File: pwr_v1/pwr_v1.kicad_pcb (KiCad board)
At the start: 2 copper layers, 166 x 166 mm, 34 parts, among them J1 Conn_01x02, J2 Conn_02x03_Counter_Clockwise, J3 Conn_01x02, J4 Conn_01x02, J5 Conn_01x02, M1 Conn_01x08_Socket, U1 LM2576S-5, U2 LM2576S-12

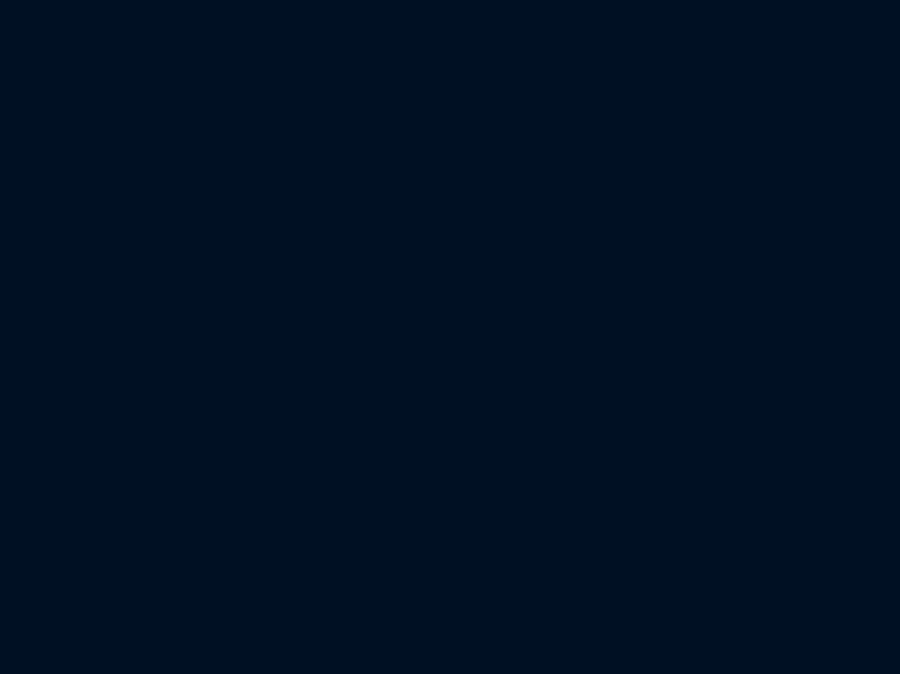
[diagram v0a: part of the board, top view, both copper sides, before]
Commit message: IMU layout updated
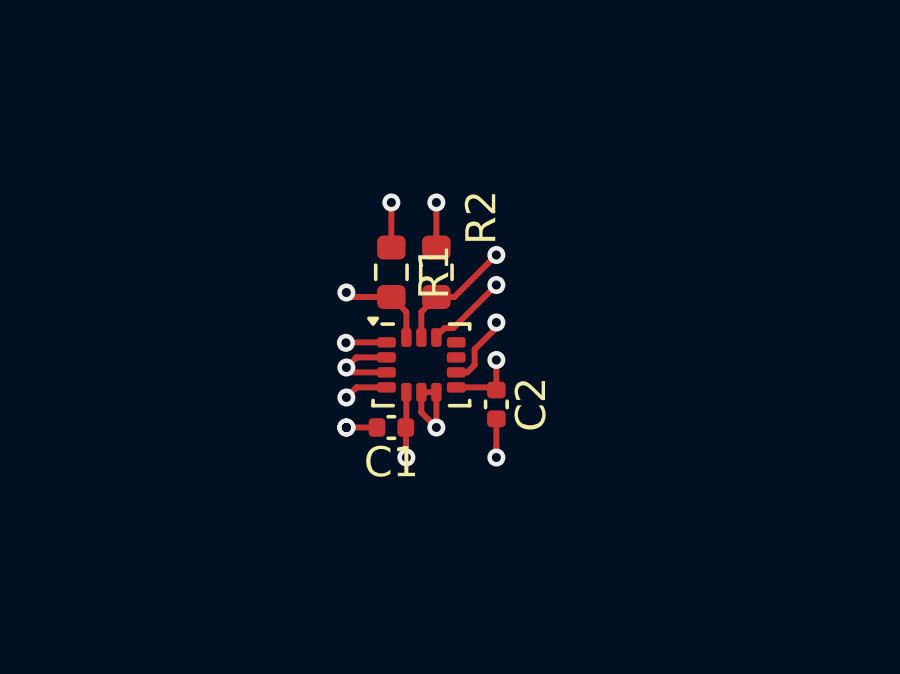
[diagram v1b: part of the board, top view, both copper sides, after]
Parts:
- added C1: 100nF, Capacitor_SMD:C_0402_1005Metric, F.Cu at (149.5, 102.5)
- added C2: 100nF, Capacitor_SMD:C_0402_1005Metric, F.Cu at (153.0, 101.7)
- added R1: 1k, Resistor_SMD:R_0603_1608Metric, F.Cu at (149.5, 97.3)
- added R2: 1k, Resistor_SMD:R_0603_1608Metric, F.Cu at (151.0, 97.3)
- added U1: LSM6DSLTR, Package_LGA:LGA-14_3x2.5mm_P0.5mm_LayoutBorder3x4y, F.Cu at (150.5, 100.4)
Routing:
- net (no net): track 0.00 -> 23.3 mm, vias 0 -> 10
- net GND: track 0.00 -> 8.58 mm, vias 124 -> 129

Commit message: Schematic and layout updated
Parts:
- removed the C1 at (149.5, 102.5)
- removed the C2 at (153.0, 101.7)
- removed D3: 1N5821, Diode_THT:D_DO-201AD_P15.24mm_Horizontal
- removed L3: 47uH, Inductor_SMD:L_0805_2012Metric
- removed REF** (x2): PinHeader_2x36_P2.54mm_Vertical_SMD, Connector_PinHeader_2.54mm:PinHeader_2x36_P2.54mm_Vertical_SMD
- removed the U1 at (150.5, 100.4)
- removed U_M1: MCT8316Z0TQRGFRQ1, MTR:RGF0040E-IPC_B
- added 1L1: 47uH, Inductor_SMD:L_0805_2012Metric, B.Cu at (147.1, 48.9)
- added 1U1: MCT8316Z0TQRGFRQ1, MTR:RGF0040E-IPC_B, B.Cu at (140.5, 52.7)
- added 2C1: 100nF, Capacitor_SMD:C_0805_2012Metric, F.Cu at (26.6, 54.5)
- added 2C2: 47nF, Capacitor_SMD:C_0603_1608Metric, F.Cu at (22.4, 47.3)
- added 2C3: 1uF, Capacitor_SMD:C_0402_1005Metric, F.Cu at (30.3, 57.0)
- added 2C4: 0u1F, Capacitor_SMD:C_0603_1608Metric, F.Cu at (22.4, 49.8)
- added 2C5: 22uF, Capacitor_SMD:C_2220_5750Metric, F.Cu at (28.6, 49.5)
- added 2C6: 22uF, Capacitor_SMD:C_0603_1608Metric, F.Cu at (22.4, 52.3)
- added 2C7: 1uF, Capacitor_SMD:C_0402_1005Metric, F.Cu at (30.3, 59.0)
- added 2L1: 47uH, Inductor_SMD:L_0805_2012Metric, F.Cu at (30.2, 38.7)
- added 2R1: 5k1, Resistor_SMD:R_0603_1608Metric_Pad0.98x0.95mm_HandSolder, F.Cu at (31.1, 54.2)
- added 2R2: 5k1, Resistor_SMD:R_0603_1608Metric, F.Cu at (22.4, 54.8)
- added 2R3: 27k, Resistor_SMD:R_0603_1608Metric, F.Cu at (22.4, 57.3)
- added 2R4: 20k, Resistor_SMD:R_0603_1608Metric, F.Cu at (22.4, 59.8)
- added 2R5: 1M, Resistor_SMD:R_0805_2012Metric, F.Cu at (26.6, 57.5)
- added 2R6: 47k, Resistor_SMD:R_0402_1005Metric, F.Cu at (29.4, 41.1)
- added 2R7: 22k, Resistor_SMD:R_0402_1005Metric, F.Cu at (29.4, 43.1)
- added 2U1: MCT8316Z0TQRGFRQ1, MTR:RGF0040E-IPC_B, F.Cu at (24.6, 41.7)
- added 3C1: 100nF, Capacitor_SMD:C_0805_2012Metric, F.Cu at (49.4, 54.5)
- added 3C2: 47nF, Capacitor_SMD:C_0603_1608Metric, F.Cu at (45.2, 47.3)
- added 3C3: 1uF, Capacitor_SMD:C_0402_1005Metric, F.Cu at (53.0, 57.0)
- added 3C4: 0u1F, Capacitor_SMD:C_0603_1608Metric, F.Cu at (45.2, 49.8)
- added 3C5: 22uF, Capacitor_SMD:C_2220_5750Metric, F.Cu at (51.4, 49.5)
- added 3C6: 22uF, Capacitor_SMD:C_0603_1608Metric, F.Cu at (45.2, 52.3)
- added 3C7: 1uF, Capacitor_SMD:C_0402_1005Metric, F.Cu at (53.0, 59.0)
- added 3L1: 47uH, Inductor_SMD:L_0805_2012Metric, F.Cu at (53.0, 38.7)
- added 3R1: 5k1, Resistor_SMD:R_0603_1608Metric_Pad0.98x0.95mm_HandSolder, F.Cu at (53.8, 54.2)
- added 3R2: 5k1, Resistor_SMD:R_0603_1608Metric, F.Cu at (45.2, 54.8)
- added 3R3: 27k, Resistor_SMD:R_0603_1608Metric, F.Cu at (45.2, 57.3)
- added 3R4: 20k, Resistor_SMD:R_0603_1608Metric, F.Cu at (45.2, 59.8)
- added 3R5: 1M, Resistor_SMD:R_0805_2012Metric, F.Cu at (49.4, 57.5)
- added 3R6: 47k, Resistor_SMD:R_0402_1005Metric, F.Cu at (52.1, 41.1)
- added 3R7: 22k, Resistor_SMD:R_0402_1005Metric, F.Cu at (52.1, 43.1)
- added 3U1: MCT8316Z0TQRGFRQ1, MTR:RGF0040E-IPC_B, F.Cu at (47.3, 41.7)
- added 4C1: 100nF, Capacitor_SMD:C_0805_2012Metric, F.Cu at (49.4, 28.7)
- added 4C2: 47nF, Capacitor_SMD:C_0603_1608Metric, F.Cu at (45.2, 21.5)
- added 4C3: 1uF, Capacitor_SMD:C_0402_1005Metric, F.Cu at (53.0, 31.2)
- added 4C4: 0u1F, Capacitor_SMD:C_0603_1608Metric, F.Cu at (45.2, 24.0)
- added 4C5: 22uF, Capacitor_SMD:C_2220_5750Metric, F.Cu at (51.4, 23.7)
- added 4C6: 22uF, Capacitor_SMD:C_0603_1608Metric, F.Cu at (45.2, 26.5)
- added 4C7: 1uF, Capacitor_SMD:C_0402_1005Metric, F.Cu at (53.0, 33.2)
- added 4L1: 47uH, Inductor_SMD:L_0805_2012Metric, F.Cu at (53.0, 12.9)
- added 4R1: 5k1, Resistor_SMD:R_0603_1608Metric_Pad0.98x0.95mm_HandSolder, F.Cu at (53.8, 28.5)
- added 4R2: 5k1, Resistor_SMD:R_0603_1608Metric, F.Cu at (45.2, 29.1)
- added 4R3: 27k, Resistor_SMD:R_0603_1608Metric, F.Cu at (45.2, 31.6)
- added 4R4: 20k, Resistor_SMD:R_0603_1608Metric, F.Cu at (45.2, 34.1)
- added 4R5: 1M, Resistor_SMD:R_0805_2012Metric, F.Cu at (49.4, 31.7)
- added 4R6: 47k, Resistor_SMD:R_0402_1005Metric, F.Cu at (52.1, 15.3)
- added 4R7: 22k, Resistor_SMD:R_0402_1005Metric, F.Cu at (52.1, 17.3)
- added 4U1: MCT8316Z0TQRGFRQ1, MTR:RGF0040E-IPC_B, F.Cu at (47.3, 15.9)
- added 5C1: 100nF, Capacitor_SMD:C_0805_2012Metric, F.Cu at (26.6, 28.7)
- added 5C2: 47nF, Capacitor_SMD:C_0603_1608Metric, F.Cu at (22.4, 21.5)
- added 5C3: 1uF, Capacitor_SMD:C_0402_1005Metric, F.Cu at (30.3, 31.2)
- added 5C4: 0u1F, Capacitor_SMD:C_0603_1608Metric, F.Cu at (22.4, 24.0)
- added 5C5: 22uF, Capacitor_SMD:C_2220_5750Metric, F.Cu at (28.6, 23.7)
- added 5C6: 22uF, Capacitor_SMD:C_0603_1608Metric, F.Cu at (22.4, 26.5)
- added 5C7: 1uF, Capacitor_SMD:C_0402_1005Metric, F.Cu at (30.3, 33.2)
- added 5L1: 47uH, Inductor_SMD:L_0805_2012Metric, F.Cu at (30.2, 12.9)
- added 5R1: 5k1, Resistor_SMD:R_0603_1608Metric_Pad0.98x0.95mm_HandSolder, F.Cu at (31.1, 28.5)
- added 5R2: 5k1, Resistor_SMD:R_0603_1608Metric, F.Cu at (22.4, 29.1)
- added 5R3: 27k, Resistor_SMD:R_0603_1608Metric, F.Cu at (22.4, 31.6)
- added 5R4: 20k, Resistor_SMD:R_0603_1608Metric, F.Cu at (22.4, 34.1)
- added 5R5: 1M, Resistor_SMD:R_0805_2012Metric, F.Cu at (26.6, 31.7)
- added 5R6: 47k, Resistor_SMD:R_0402_1005Metric, F.Cu at (29.4, 15.3)
- added 5R7: 22k, Resistor_SMD:R_0402_1005Metric, F.Cu at (29.4, 17.3)
- added 5U1: MCT8316Z0TQRGFRQ1, MTR:RGF0040E-IPC_B, F.Cu at (24.6, 15.9)
- added BAT1: Conn_01x02, TerminalBlock_4Ucon:TerminalBlock_4Ucon_1x02_P3.50mm_Horizontal, F.Cu at (61.1, 48.5)
- added C12: 100nF, Capacitor_SMD:C_0402_1005Metric, F.Cu at (149.4, 102.5)
- added C13: 100nF, Capacitor_SMD:C_0402_1005Metric, F.Cu at (153.0, 101.8)
- added CN11: Conn_02x36_Odd_Even, Connector_PinHeader_2.54mm:PinHeader_2x36_P2.54mm_Vertical_SMD, F.Cu at (131.8, 121.0)
- added CN12: Conn_02x36_Odd_Even, Connector_PinHeader_2.54mm:PinHeader_2x36_P2.54mm_Vertical_SMD, F.Cu at (177.2, 116.0)
- added D1: 1N5821, Diode_THT:D_DO-201AD_P15.24mm_Horizontal, F.Cu at (60.4, 40.7)
- added M2: Conn_01x08_Socket, Connector_PinHeader_2.54mm:PinHeader_1x08_P2.54mm_Vertical_SMD_Pin1Left, F.Cu at (16.4, 48.5)
- added M3: Conn_01x08_Socket, Connector_PinHeader_2.54mm:PinHeader_1x08_P2.54mm_Vertical_SMD_Pin1Left, F.Cu at (39.2, 48.5)
- added M4: Conn_01x08_Socket, Connector_PinHeader_2.54mm:PinHeader_1x08_P2.54mm_Vertical_SMD_Pin1Left, F.Cu at (39.2, 22.8)
- added M5: Conn_01x08_Socket, Connector_PinHeader_2.54mm:PinHeader_1x08_P2.54mm_Vertical_SMD_Pin1Left, F.Cu at (16.4, 22.8)
- added R3: 1k, Resistor_SMD:R_0603_1608Metric, F.Cu at (1.50, 0.76)
- added U4: LSM6DSLTR, Package_LGA:LGA-14_3x2.5mm_P0.5mm_LayoutBorder3x4y, F.Cu at (150.5, 100.5)
- 1C1: footprint Capacitor_SMD:C_0805_2012Metric -> Capacitor_SMD:C_0402_1005Metric
- 1C2, 1C4, 1C6: footprint Capacitor_SMD:C_0603_1608Metric -> Capacitor_SMD:C_0402_1005Metric
- 1C7: footprint Capacitor_SMD:C_1206_3216Metric -> Capacitor_SMD:C_0402_1005Metric
- C3: footprint Capacitor_SMD:CP_Elec_10x10.5 -> Capacitor_SMD:CP_Elec_8x10.5
- C4: footprint Capacitor_SMD:CP_Elec_8x10.5 -> Capacitor_SMD:CP_Elec_10x10.5
- L1: footprint Inductor_SMD:L_TaiTech_TMPC1265_13.5x12.5mm -> Inductor_SMD:L_Sunlord_MWSA1206S-101
- L2: footprint Inductor_SMD:L_Sunlord_MWSA1206S-101 -> Inductor_SMD:L_TaiTech_TMPC1265_13.5x12.5mm
- R1: value 1k -> R_Small_US
- moved 1C7 194.2 mm to (135.4, 55.2)
- moved 1C3 193.5 mm to (146.3, 54.2)
- moved 1C4 192.0 mm to (145.1, 55.2)
- moved 1C2 192.0 mm to (146.4, 51.9), turned to 180 degrees
- moved 1C6 191.5 mm to (146.6, 46.4), turned to 180 degrees
- moved 1R3 190.8 mm to (139.9, 42.9), turned to 0 degrees
- moved 1R2 189.6 mm to (145.2, 44.0), turned to -90 degrees
- moved 1C1 189.3 mm to (140.3, 46.0), turned to 180 degrees
- moved 1R7 189.1 mm to (136.9, 45.5)
- moved 1R5 188.9 mm to (132.8, 53.0), turned to 180 degrees
- moved 1R6 188.9 mm to (135.7, 45.5)
- moved 1R1 188.1 mm to (131.8, 56.0), turned to -90 degrees
- moved 1R4 186.9 mm to (139.9, 44.6), turned to 180 degrees
- moved 1C5 186.4 mm to (150.5, 58.1), turned to -90 degrees
- moved M1 177.6 mm to (163.7, 50.4)
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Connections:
- net /MotorDrivers/AVDD renamed /MotorDriver1/AVDD
- net /MotorDrivers/SW_BK renamed /MotorDriver1/SW_BK
- net /MotorDrivers/VM renamed +24V
- net 12V renamed +12V
- 1C1 pad 2: GNDREF -> GND
- 1C4 pad 2: GNDREF -> GND
- 1C5 pad 2: GNDREF -> GND
- 1C6 pad 2: GNDREF -> /MotorDriver1/GND_BK
- 1C7 pad 2: GNDREF -> GND
- 1R1 pad 2: /MotorDrivers/nFault -> +5V
- 1R2 pad 2: /MotorDrivers/FGOUT -> /MotorDriver1/FGOUT
- 1R4 pad 2: GNDREF -> GND
- C3 pad 1: 5V -> +5V
- L1 pad 2: 5V -> +5V
- M1 pad 1: /MotorDrivers/U -> /MotorDriver1/U
- M1 pad 2: /MotorDrivers/V -> /MotorDriver1/V
- M1 pad 3: /MotorDrivers/W -> /MotorDriver1/W
- M1 pad 4: GNDREF -> /MotorDriver1/GND_BK
- M1 pad 5: /MotorDrivers/H2 -> /MotorDriver1/H2
- M1 pad 6: /MotorDrivers/H1 -> /MotorDriver1/H1
- M1 pad 7: /MotorDrivers/H3 -> /MotorDriver1/H3
- R1 pad 1: (no net) -> /Battery Supervisor/B1
- R1 pad 2: (no net) -> Net-(D3-A)
- R2 pad 1: (no net) -> /IMU/3V3
- R2 pad 2: (no net) -> /IMU/SCL
- U1 pad 4: 5V -> +5V
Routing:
- net /MotorDriver1/AVDD: track 0.00 -> 25.4 mm, vias 0 -> 5
- net (no net): track 23.3 -> 0.00 mm, vias 10 -> 0
- net +24V: track 0.00 -> 13.9 mm
- net GND: track 8.58 -> 21.8 mm, vias 129 -> 136
- net +5V: track 0.00 -> 9.76 mm, vias 0 -> 1
- net /MotorDriver1/GND_BK: track 0.00 -> 7.00 mm
- net Net-(1U1-ILIM): track 0.00 -> 6.38 mm
- net /IMU/3V3: track 0.00 -> 6.31 mm, vias 0 -> 3
- net Net-(1U1-SLEW): track 0.00 -> 5.75 mm
- net /MotorDriver1/W: track 0.00 -> 5.70 mm
- net /MotorDriver1/V: track 0.00 -> 5.70 mm
- net /MotorDriver1/U: track 0.00 -> 5.70 mm
- net /MotorDriver1/FGOUT: track 0.00 -> 5.64 mm
- net Net-(1U1-ADVANCE): track 0.00 -> 5.22 mm
- net /MotorDriver1/SW_BK: track 0.00 -> 5.19 mm, vias 0 -> 1
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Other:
- copper layers 2 -> 6

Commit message: Sch and Layout updated; Added batt sup ckt, placed and routed all motor drivers.
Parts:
- removed J1: Conn_01x02, TerminalBlock_4Ucon:TerminalBlock_4Ucon_1x02_P3.50mm_Horizontal
- removed J2: Conn_02x03_Counter_Clockwise, Connector_PinHeader_2.54mm:PinHeader_1x02_P2.54mm_Vertical
- removed J3, J4, J5: Conn_01x02, Connector_PinHeader_2.54mm:PinHeader_1x02_P2.54mm_Vertical
- added R10: 11k, Resistor_SMD:R_0402_1005Metric, F.Cu at (114.1, 58.5)
- added R11: 3k, Resistor_SMD:R_0402_1005Metric, F.Cu at (111.0, 60.0)
- added R12: 11k, Resistor_SMD:R_0402_1005Metric, F.Cu at (114.0, 60.0)
- added R13: 3k, Resistor_SMD:R_0402_1005Metric, F.Cu at (111.0, 61.1)
- added R14: 11k, Resistor_SMD:R_0402_1005Metric, F.Cu at (114.0, 61.1)
- added R4: 11k, Resistor_SMD:R_0402_1005Metric, F.Cu at (114.0, 53.5)
- added R5: 3k, Resistor_SMD:R_0402_1005Metric, F.Cu at (111.0, 55.5)
- added R6: 11k, Resistor_SMD:R_0402_1005Metric, F.Cu at (114.0, 55.5)
- added R7: 3k, Resistor_SMD:R_0402_1005Metric, F.Cu at (111.0, 57.0)
- added R8: 11k, Resistor_SMD:R_0402_1005Metric, F.Cu at (114.1, 57.0)
- added R9: 3k, Resistor_SMD:R_0402_1005Metric, F.Cu at (111.0, 58.5)
- 1R1: footprint Resistor_SMD:R_0603_1608Metric_Pad0.98x0.95mm_HandSolder -> Resistor_SMD:R_0603_1608Metric
- 2C1, 3C1, 4C1, 5C1: footprint Capacitor_SMD:C_0805_2012Metric -> Capacitor_SMD:C_0402_1005Metric; moved to B.Cu
- 2C2, 2C4, 2C6, 3C2, 3C4, 3C6, 4C2, 4C4, 4C6, 5C2, 5C4, 5C6: footprint Capacitor_SMD:C_0603_1608Metric -> Capacitor_SMD:C_0402_1005Metric; moved to B.Cu
- 2C3, 2C5, 2C7, 2L1, 2R2, 2R3, 2R4, 2R5, 2R6, 2R7, 2U1, 3C3, 3C5, 3C7, 3L1, 3R2, 3R3, 3R4, 3R5, 3R6, 3R7, 3U1, 4C3, 4C5, 4C7, 4L1, 4R2, 4R3, 4R4, 4R5, 4R6, 4R7, 4U1, 5C3, 5C5, 5C7, 5L1, 5R2, 5R3, 5R4, 5R5, 5R6, 5R7, 5U1: moved to B.Cu
- 2R1, 3R1, 4R1, 5R1: footprint Resistor_SMD:R_0603_1608Metric_Pad0.98x0.95mm_HandSolder -> Resistor_SMD:R_0603_1608Metric; moved to B.Cu
- BAT1: value Conn_01x02 -> XT60; footprint TerminalBlock_4Ucon:TerminalBlock_4Ucon_1x02_P3.50mm_Horizontal -> Connector_AMASS:AMASS_XT60-M_1x02_P7.20mm_Vertical
- M1: footprint Connector_PinHeader_2.54mm:PinHeader_1x08_P2.54mm_Vertical_SMD_Pin1Left -> Connector_PinHeader_2.54mm:PinHeader_1x08_P2.54mm_Vertical; moved to F.Cu
- M2, M3, M4, M5: footprint Connector_PinHeader_2.54mm:PinHeader_1x08_P2.54mm_Vertical_SMD_Pin1Left -> Connector_PinHeader_2.54mm:PinHeader_1x08_P2.54mm_Vertical
- R1: value R_Small_US -> 3k; footprint Resistor_SMD:R_0603_1608Metric -> Resistor_SMD:R_0402_1005Metric
- moved M5 392.6 mm to (374.4, 184.1), turned to -90 degrees
- moved 5C2 385.6 mm to (378.1, 170.4), turned to 90 degrees
- moved 5C5 384.7 mm to (381.8, 176.4), turned to -90 degrees
- moved 5C4 384.5 mm to (376.4, 174.2), turned to -90 degrees
- moved 5C6 381.4 mm to (377.9, 164.8), turned to 180 degrees
- moved 5L1 380.9 mm to (378.4, 167.2), turned to 90 degrees
- moved 5U1 380.3 mm to (371.8, 171.1), turned to 180 degrees
- moved 5R2 377.2 mm to (375.2, 162.3), turned to -90 degrees
- moved 5C3 375.4 mm to (378.1, 172.4), turned to -90 degrees
- moved 5R3 372.1 mm to (371.2, 161.2)
- moved 5R4 371.8 mm to (371.2, 162.9), turned to 180 degrees
- moved 5C1 370.7 mm to (371.6, 164.3), turned to 180 degrees
- moved 5R7 369.2 mm to (368.2, 163.9), turned to 90 degrees
- moved 5R6 368.9 mm to (367.0, 163.9), turned to 90 degrees
- moved 5R5 368.2 mm to (366.1, 174.2), turned to -90 degrees
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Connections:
- net +12V renamed 12V
- net /IMU/3V3 renamed /3V3
- net /RF/MISO renamed /MISO
- net /RF/SCK renamed /SCK
- 1C3 pad 2: +24V -> VBAT
- 1C4 pad 1: +24V -> VBAT
- 1C5 pad 1: +24V -> VBAT
- 1R1 pad 2: +5V -> 5V
- 1U1 pad 10: +24V -> VBAT
- 1U1 pad 11: +24V -> VBAT
- 1U1 pad 22: +5V -> 5V
- 1U1 pad 9: +24V -> VBAT
- 2C1 pad 2: -24V -> GND
- 2C3 pad 2: +24V -> VBAT
- 2C4 pad 1: +24V -> VBAT
- 2C4 pad 2: -24V -> GND
- 2C5 pad 1: +24V -> VBAT
- 2C5 pad 2: -24V -> GND
- 2C7 pad 2: -24V -> GND
- 2R1 pad 2: +5V -> 5V
- 2R4 pad 2: -24V -> GND
- 2U1 pad 10: +24V -> VBAT
- 2U1 pad 11: +24V -> VBAT
- 2U1 pad 12: -24V -> GND
- 2U1 pad 15: -24V -> GND
- 2U1 pad 18: -24V -> GND
- 2U1 pad 2: -24V -> GND
- 2U1 pad 21: -24V -> GND
- 2U1 pad 22: +5V -> 5V
- 2U1 pad 26: -24V -> GND
- 2U1 pad 41: -24V -> GND
- 2U1 pad 9: +24V -> VBAT
- 3C1 pad 2: -24V -> GND
- 3C3 pad 2: +24V -> VBAT
- 3C4 pad 1: +24V -> VBAT
- 3C4 pad 2: -24V -> GND
- 3C5 pad 1: +24V -> VBAT
- 3C5 pad 2: -24V -> GND
- 3C7 pad 2: -24V -> GND
- 3R1 pad 2: +5V -> 5V
- 3R4 pad 2: -24V -> GND
- 3U1 pad 10: +24V -> VBAT
- 3U1 pad 11: +24V -> VBAT
- 3U1 pad 12: -24V -> GND
- 3U1 pad 15: -24V -> GND
- 3U1 pad 18: -24V -> GND
- 3U1 pad 2: -24V -> GND
- 3U1 pad 21: -24V -> GND
- 3U1 pad 22: +5V -> 5V
- 3U1 pad 26: -24V -> GND
- 3U1 pad 41: -24V -> GND
- 3U1 pad 9: +24V -> VBAT
- 4C1 pad 2: -24V -> GND
- 4C3 pad 2: +24V -> VBAT
- 4C4 pad 1: +24V -> VBAT
- 4C4 pad 2: -24V -> GND
- 4C5 pad 1: +24V -> VBAT
- 4C5 pad 2: -24V -> GND
- 4C7 pad 2: -24V -> GND
- 4R1 pad 2: +5V -> 5V
- 4R4 pad 2: -24V -> GND
- 4U1 pad 10: +24V -> VBAT
- 4U1 pad 11: +24V -> VBAT
- 4U1 pad 12: -24V -> GND
- 4U1 pad 15: -24V -> GND
- 4U1 pad 18: -24V -> GND
- 4U1 pad 2: -24V -> GND
- 4U1 pad 21: -24V -> GND
- 4U1 pad 22: +5V -> 5V
- 4U1 pad 26: -24V -> GND
- 4U1 pad 41: -24V -> GND
- 4U1 pad 9: +24V -> VBAT
- 5C1 pad 2: -24V -> GND
- 5C3 pad 2: +24V -> VBAT
- 5C4 pad 1: +24V -> VBAT
- 5C4 pad 2: -24V -> GND
- 5C5 pad 1: +24V -> VBAT
- 5C5 pad 2: -24V -> GND
- 5C7 pad 2: -24V -> GND
- 5R1 pad 2: +5V -> 5V
- 5R4 pad 2: -24V -> GND
- 5U1 pad 10: +24V -> VBAT
- 5U1 pad 11: +24V -> VBAT
- 5U1 pad 12: -24V -> GND
- 5U1 pad 15: -24V -> GND
- 5U1 pad 18: -24V -> GND
- 5U1 pad 2: -24V -> GND
- 5U1 pad 21: -24V -> GND
- 5U1 pad 22: +5V -> 5V
- 5U1 pad 26: -24V -> GND
- 5U1 pad 41: -24V -> GND
- 5U1 pad 9: +24V -> VBAT
- C3 pad 1: +5V -> 5V
- CN11 pad 20: unconnected-(CN11-Pin_20-Pad20) -> GND
- CN11 pad 6: unconnected-(CN11-Pin_6-Pad6) -> 5V
- CN12 pad 15: unconnected-(CN12-Pin_15-Pad15) -> /MOSI
- L1 pad 2: +5V -> 5V
- R1 pad 2: Net-(D3-A) -> /Battery Supervisor/O1
- U1 pad 4: +5V -> 5V
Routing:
- net GND: track 21.8 -> 101.7 mm, vias 136 -> 183
- net 5V: track 0.00 -> 16.2 mm, vias 0 -> 10
- net /MotorDriver4/AVDD: track 0.00 -> 16.1 mm, vias 0 -> 9
- net /MotorDriver2/AVDD: track 0.00 -> 16.1 mm, vias 0 -> 9
- net /MotorDriver3/AVDD: track 0.00 -> 16.1 mm, vias 0 -> 9
- net +24V: track 13.9 -> 0.00 mm
- net /MotorDriver5/AVDD: track 0.00 -> 12.2 mm, vias 0 -> 7
- net /MotorDriver4/SW_BK: track 0.00 -> 12.1 mm, vias 0 -> 1
- net /MotorDriver2/SW_BK: track 0.00 -> 12.1 mm, vias 0 -> 1
- net /MotorDriver3/SW_BK: track 0.00 -> 12.1 mm, vias 0 -> 1
- net /MotorDriver5/SW_BK: track 0.00 -> 11.7 mm, vias 0 -> 1
- net /MotorDriver1/AVDD: track 25.4 -> 14.1 mm, vias 5 -> 9
- net /MotorDriver3/U: track 0.00 -> 10.0 mm
- net /MotorDriver5/U: track 0.00 -> 10.0 mm
- net /MotorDriver4/U: track 0.00 -> 10.0 mm
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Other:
- copper layers 6 -> 4

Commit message: Schematic and layout updated; Motor driver alignments and planes;  Few components updated
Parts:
- added J_IR1: Connector_Generic:Conn_01x05, Connector_PinHeader_2.54mm:PinHeader_1x05_P2.54mm_Vertical, F.Cu at (155.3, 22.2)
- added J_RF1: Conn_02x04_Counter_Clockwise, Connector_PinHeader_2.54mm:PinHeader_2x04_P2.54mm_Vertical, F.Cu at (103.8, 35.8)
- added REF**: ST_Morpho_Connector_144_STLink, Module:ST_Morpho_Connector_144_STLink, F.Cu at (118.0, 65.1)
- M1, M2, M3, M4, M5: footprint Connector_PinHeader_2.54mm:PinHeader_1x08_P2.54mm_Vertical -> Connector_Molex:Molex_KK-254_AE-6410-08A_1x08_P2.54mm_Vertical
- moved CN11 17.1 mm to (119.2, 109.5)
- moved R14 11.2 mm to (104.7, 67.4)
- moved R1 11.2 mm to (101.6, 59.8)
- moved R10 11.2 mm to (104.8, 64.8)
- moved R11 11.2 mm to (101.6, 66.2)
- moved R12 11.2 mm to (104.7, 66.2)
- moved R4 11.2 mm to (104.7, 59.8)
- moved R5 11.2 mm to (101.6, 61.8)
- moved R6 11.2 mm to (104.7, 61.8)
- moved R7 11.2 mm to (101.6, 63.2)
- moved R9 11.2 mm to (101.6, 64.8)
- moved R13 11.2 mm to (101.6, 67.3)
- moved R8 11.2 mm to (104.8, 63.2)
- moved CN12 7.11 mm to (180.2, 109.5)
- moved C12 0.58 mm to (148.9, 102.7)
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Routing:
- net GND: track 101.7 -> 142.8 mm, vias 183 -> 264
- net /MotorDriver1/AVDD: track 14.1 -> 22.9 mm, vias 9 -> 13
- net /MotorDriver2/AVDD: track 16.1 -> 13.0 mm, vias 9 -> 8
- net /MotorDriver3/AVDD: track 16.1 -> 13.6 mm, vias 9 -> 8
- net /MotorDriver4/AVDD: track 16.1 -> 13.6 mm, vias 9 -> 8
- net /MotorDriver5/AVDD: track 12.2 -> 13.0 mm, vias 7 -> 8

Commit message: Schematic updated; Layout updated; STM PinMappings file added
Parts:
- moved 3C1 335.3 mm to (41.9, 131.0)
- moved 3C2 335.3 mm to (48.0, 136.9)
- moved 3C3 335.3 mm to (48.4, 139.1)
- moved 3C4 335.3 mm to (46.7, 140.8)
- moved 3C5 335.3 mm to (52.1, 143.1)
- moved 3C6 335.3 mm to (48.2, 131.4)
- moved 3C7 335.3 mm to (36.9, 137.9)
- moved 3L1 335.3 mm to (48.7, 133.9)
- moved 3R1 335.3 mm to (37.2, 143.5)
- moved 3R2 335.3 mm to (45.6, 129.0)
- moved 3R3 335.3 mm to (41.5, 127.9)
- moved 3R4 335.3 mm to (41.5, 129.6)
- moved 3R5 335.3 mm to (36.5, 140.8)
- moved 3R6 335.3 mm to (37.3, 130.5)
- moved 3R7 335.3 mm to (38.5, 130.5)
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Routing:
- net /MotorDriver1/AVDD: track 22.9 -> 16.4 mm, vias 13 -> 9
- net GND: track 142.8 -> 145.4 mm, vias 264 -> 253
- net /MotorDriver5/AVDD: track 13.0 -> 14.9 mm, vias 8 -> 9
- net /MotorDriver3/AVDD: track 13.6 -> 15.4 mm, vias 8 -> 9
- net /MotorDriver4/AVDD: track 13.6 -> 15.3 mm, vias 8 -> 9
- net /MotorDriver2/AVDD: track 13.0 -> 14.7 mm, vias 8 -> 9
- net /IMU/INT2: track 2.43 -> 1.52 mm
- net /IMU/SDA: track 3.12 -> 4.01 mm
- net /IMU/CS: track 2.75 -> 2.12 mm
- net /3V3: track 7.81 -> 7.30 mm
